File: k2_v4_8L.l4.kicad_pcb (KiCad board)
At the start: 8 copper layers, 120 x 46 mm, 42 parts, among them J11 J_EC_HEADER, J12 J_12V_IN, J13 J_SWD, J2 SlimSAS_x8_SFF8654, J3 MCIO_4i_SFF1016, J4 MCIO_4i_SFF1016, J6 J_PWR_CTRL, J9 J_OOB_HEADER, U1 STM32G0B1CBT6, U2 DCDC_12V_3V3, U4 BAT54C, U5 OPTO_LTV356T, U6 DS320PR1601

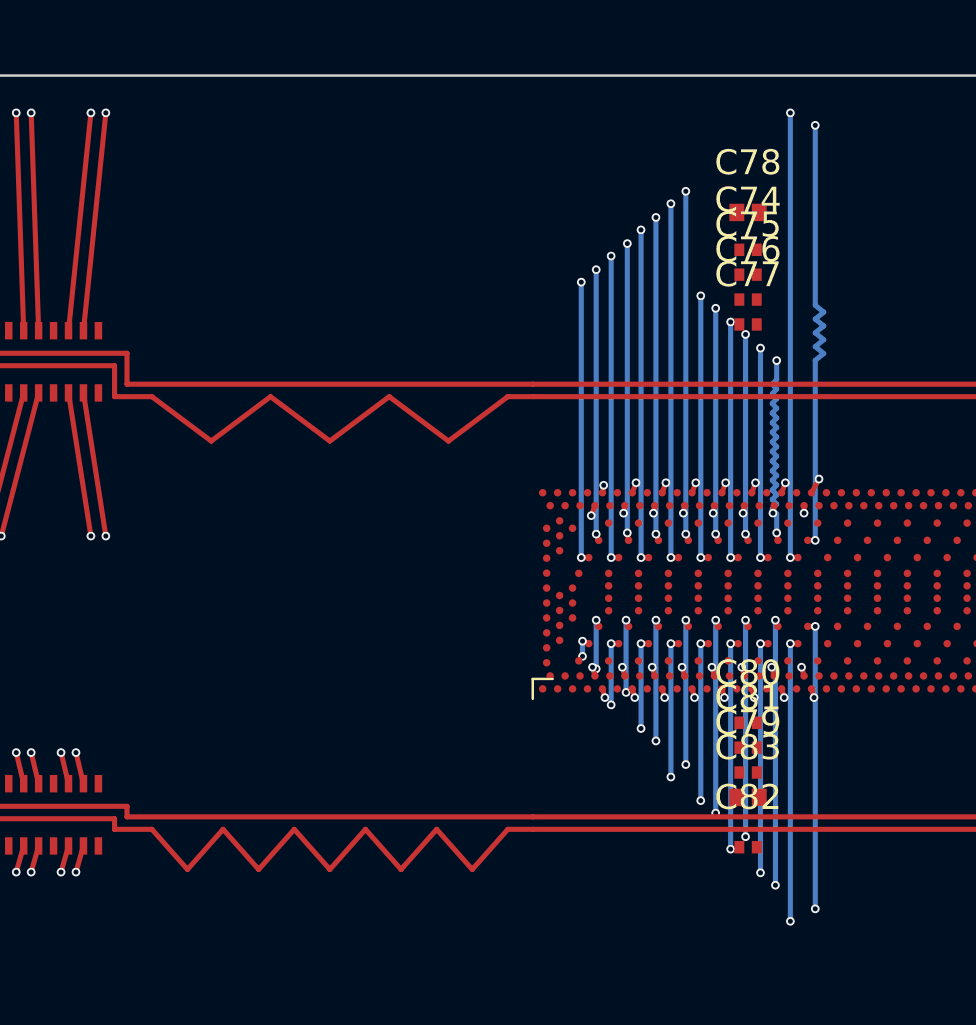
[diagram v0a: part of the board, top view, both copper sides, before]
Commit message: CO-67..CO-69: 【L2 叠层分配】方案(a) 全链执行 + SI 按层加权电气等长整改；boundary v1.36
CO-67（L2 定层裁定）：方案(a)（In5 GND→信号）vs 历史红线「平面层用途不得改信号」的一次性张力裁定。
机判不变量全不变（层数 8 / 平面数 4 / 电源域划分 3×GND+1×P3V3 / 信号层 4）⇒ 归口 L2（叠层分配），
无需 L1 升裁；带 ECN + 版本 bump + 全链重跑 + 重新对抗评审控制。四冻结源 4/4 MATCH。

CO-68（铜厚自洽修正 + 版本化输入）：修正 CO-66 闭合式未扣铜厚（0.175）之误 ⇒ 介质预算 1.425。
设计点：外层微带 w=0.205/h=0.1164，内层对称带状线 w=0.16/b=0.50，闭合 1.6000，各层 85±10%。
发射 LID REV6（signal=F/In2/In5/B；In1/In3/In6=GND，In4=P3V3）与 SPEC rev-5（纯加性；阈值未改）。

CO-69（引擎 bump + 全链）：
- 引擎 LAYER_PALETTE=F/In2/In5/B、In6→In5 全量、F.spec→rev-5、F.layer_intent→rev6、rev W3-CN.41；
  新增 CO16-ALLOC.7（stub 层 In6→In5，4 页；不触碰 CO-60 候选 v6 2ebda54c）。
- L4 applier 改按层线宽（F/B 0.205、In2/In5 0.16）；L5 判据升级为按层加权电气长度（CO-62 §4）。
- 全链：G4 FEASIBLE_ALL 87ef07f2 / G5 PASS 14f6d92e / G6 PASS 板 0e636a67（68 网 2523 段 252 via）
  / G7 FAB ok + DFM PASS new=0 + SI PASS。
- SI 电气等长：升级前 max 0.9807 > 0.15 ⇒ FAIL（REFCLK1 P 全 F.Cu vs N F.Cu+In2 8.745mm）；
  L2 等长整改（补偿目标由物理长度改为层加权电气长度）⇒ max 0.1300 ≤ 0.15 ⇒ PASS；
  物理量报告 max 1.1046mm（层补偿之预期）。
- 全链连跑 ×2：11 件产出逐字节一致。四冻结源 4/4 MATCH；历史 SPEC/分配件未动。
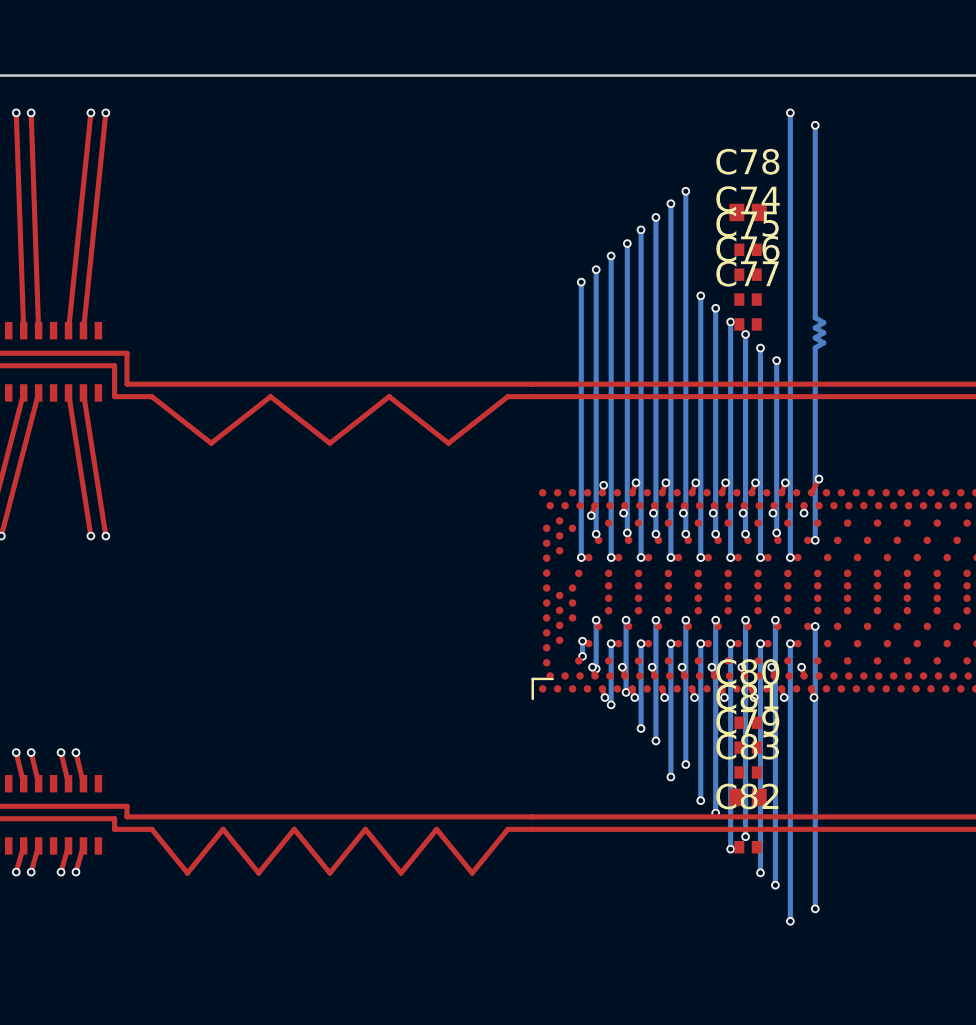
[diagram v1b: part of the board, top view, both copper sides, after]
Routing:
- net PCIE_REFCLK1_P: track 93.6 -> 94.7 mm
- net PCIE_UP_OUT4_N_J2: track 78.0 -> 77.4 mm

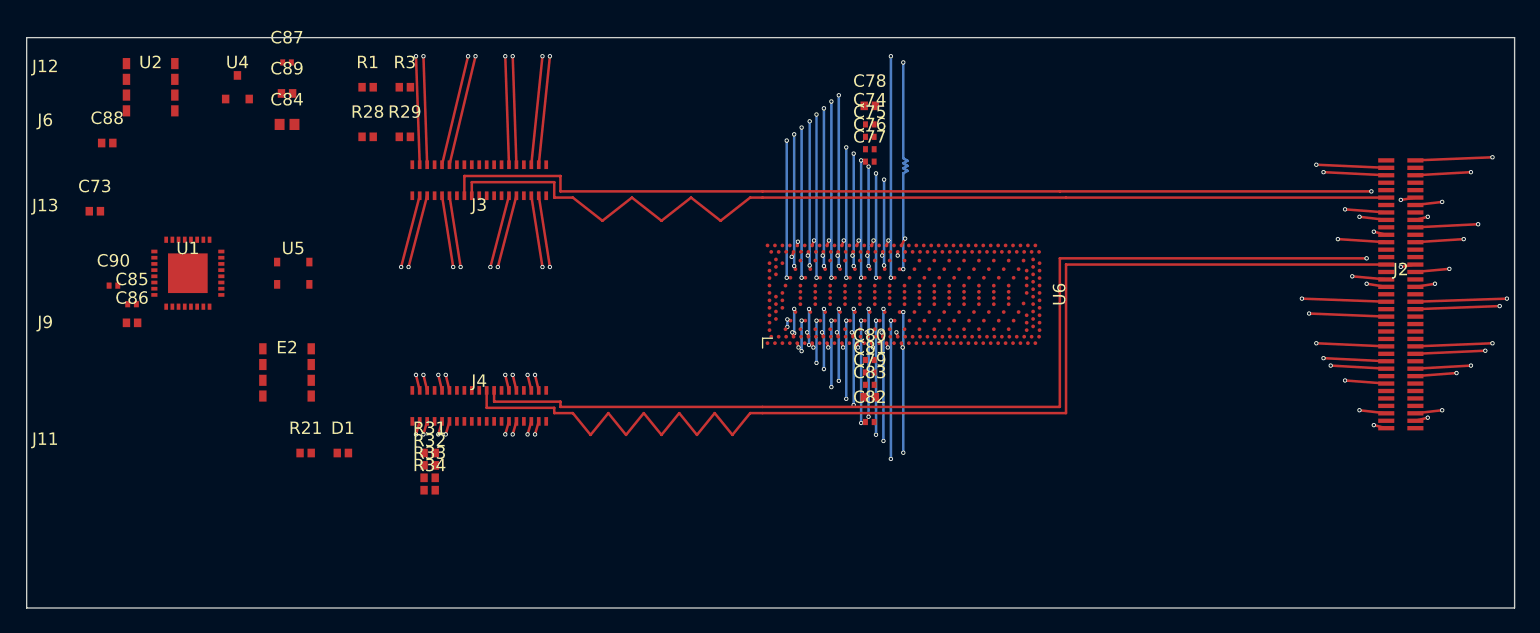
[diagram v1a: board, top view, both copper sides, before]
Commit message: CO-133（L2 自裁 · 施工期物理施加）：rev-18 声明 PDN 铜落板 + 板实合规机判 + 全链重基线
施加（零自由度：坐标逐字取自 SPEC，无搜索/无随机）：
- 板 k2_v4_8L.l4.kicad_pcb 0e636a67c1472462 → a3ce9ab803045a0a = 图纸 2708 track/252 via + PDN 185 短段/241 via/9 zone
  （3×GND 平面 In1/In3/In6 + 6×In4 电源区；3 区 fill_priority=1）
- 项目内 applier 追加④ 幂等 purge-then-add（删本阶段将重发的 PDN 网铜；pcbnew 删除改走 RemoveNative
  —— `Remove` 会泄漏 ZONE*/PCB_TRACK* 并使 GetTracks() 退化为不可迭代 SwigPyObject）
  + CO-49 canonicalize ⇒ 净板/已施工板两次投喂同一字节（实测重跑后板 sha 不变）；只回写板，不污染受控 .kicad_pro

机判（A/B/C/D 全 PASS）：A 板实 vs SPEC 逐项相等；B kicad-cli --severity-all 违规类型逐项同（42/42）、
未连项 348→179；C 幂等同一字节；D 图纸 2523 段/252 via 逐条不变。L4-A..F viol 0；L5 DFM new=0/SI 0.1300。

连带更正（显式登记：register 3 条 + co133 记录 findings）：
- co91 via-via 孔缘分支多扣一次 via_r（与其 drc_rules geometry_translation 相悖）⇒ 施工后 14 项假阳性；
  更正后 0/0（真值 +0.284 / req 0.25）；co104 replay 场景改排除计划自身网 + V3 断言/verdict 改数据派生
  （残留：canonical replay 3 vs 声明 blocked 4 ⇒ 声明偏保守 1 项，无功能影响）
- provenance pin：co105←co98 随重跑刷新；co111←l5_si / co118←co95 属 point-in-time ⇒ co120 EXEMPT 明列理由

重基线（全 PASS）：co124（register 14 项）/co95 55/55/co98 55/0/0/co91/co97/co98/co99/co102 local +0/
co104 ACCEPT_L2_NO_HDI/co105 4/4/co106 INDETERMINATE/co120（match 6·exempt 5·stale 0）/co88/co78/co81/co84/
co87/co69 10/10/co77（boundary v1.86 全量引用同步）；G4 6ad2ff97101cbc53 / G5 6d22980eec78094a 不动。

未决：非执行者复评（本件 + rev-18 新基线，禁自评）；owner ③ 0.875 口径批准；外部输入（板厂券/SI9000、PM 压降·热）。
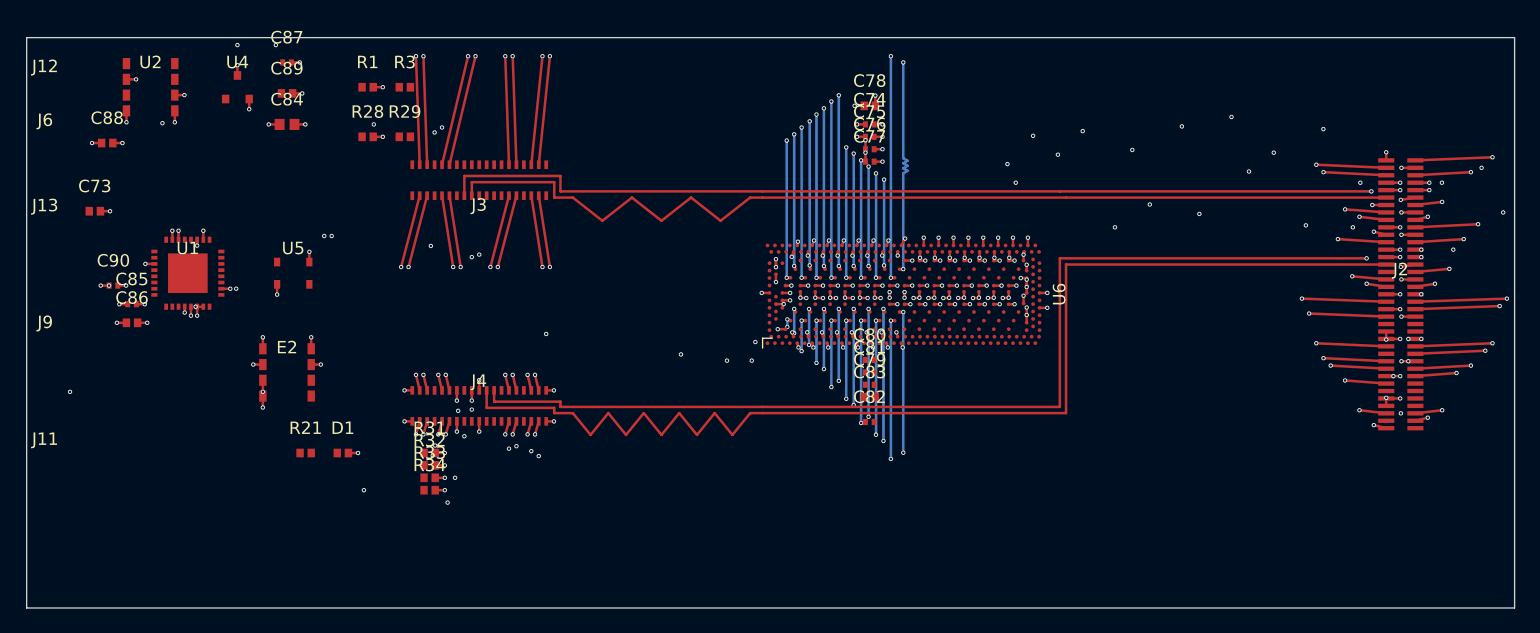
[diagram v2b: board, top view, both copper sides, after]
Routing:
- net GND: track 0.00 -> 90.6 mm, vias 0 -> 169
- net P3V3: track 0.00 -> 20.9 mm, vias 0 -> 41
- net MCU_VDD: track 0.00 -> 7.55 mm, vias 0 -> 16
- net P3V3_AUX: track 0.00 -> 3.00 mm, vias 0 -> 12
- net 12V_IN: track 0.00 -> 2.47 mm, vias 0 -> 3
- added copper zone on In4.Cu, net 12V_IN
- added copper zone on In1.Cu, net GND
- added copper zone on In3.Cu, net GND
- added copper zone on In6.Cu, net GND
- added copper zone on In4.Cu, net MCU_VDD
- added copper zone on In4.Cu, net P3V3
- added copper zone on In4.Cu, net P3V3_AUX
